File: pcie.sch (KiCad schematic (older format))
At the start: 20 parts

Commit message: sch: Add PCIe power supply
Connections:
- net labels added: +1V5_PCI, +3V3_PCI
- net labels removed: +1V5
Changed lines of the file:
@@
 Connection ~ 3900 2000
 Wire Wire Line
-	2800 2600 2500 2600
-Wire Wire Line
-	2500 2600 2500 1800
+	2800 2600 2400 2600
+Wire Wire Line
+	2400 2600 2400 1800
 $Comp
 L power:+12V #PWR?
@@
 	1    0    0    -1
 $EndComp
-$Comp
-L power:+3V3 #PWR?
-U 1 1 5C9785AC
-P 2500 1800
-F 0 "#PWR?" H 2500 1650 50  0001 C CNN
-F 1 "+3V3" H 2515 1973 50  0000 C CNN
-F 2 "" H 2500 1800 50  0001 C CNN
-F 3 "" H 2500 1800 50  0001 C CNN
-	1    2500 1800
-	1    0    0    -1
-$EndComp
-Wire Wire Line
-	2800 2800 2500 2800
-Wire Wire Line
-	2500 2800 2500 2600
-Connection ~ 2500 2600
+Wire Wire Line
+	2800 2800 2400 2800
+Wire Wire Line
+	2400 2800 2400 2600
+Connection ~ 2400 2600
 $Comp
 L power:+12V #PWR?
@@
 	1    0    0    -1
 $EndComp
-$Comp
-L power:+3V3 #PWR?
-U 1 1 5C9785BB
-P 4100 1800
-F 0 "#PWR?" H 4100 1650 50  0001 C CNN
-F 1 "+3V3" H 4115 1973 50  0000 C CNN
-F 2 "" H 4100 1800 50  0001 C CNN
-F 3 "" H 4100 1800 50  0001 C CNN
-	1    4100 1800
-	1    0    0    -1
-$EndComp
-Wire Wire Line
-	3800 2700 4100 2700
-Wire Wire Line
-	4100 2700 4100 1800
-Wire Wire Line
-	3800 2800 4100 2800
-Wire Wire Line
-	4100 2800 4100 2700
-Connection ~ 4100 2700
+Wire Wire Line
+	3800 2700 4200 2700
+Wire Wire Line
+	4200 2700 4200 1800
+Wire Wire Line
+	3800 2800 4200 2800
+Wire Wire Line
+	4200 2800 4200 2700
+Connection ~ 4200 2700
 Wire Wire Line
 	8100 3000 6550 3000
@@
 Wire Wire Line
 	10150 3200 9400 3200
-Text Label 9850 3100 0    50   ~ 0
+Text Label 9750 3100 0    50   ~ 0
 SCL
-Text Label 9850 3200 0    50   ~ 0
+Text Label 9750 3200 0    50   ~ 0
 SDA
 Wire Bus Line
@@
 Wire Wire Line
 	3800 1900 4550 1900
-Text Label 4150 1900 0    50   ~ 0
+Text Label 4250 1900 0    50   ~ 0
 X4_PRSNT
 $Comp
@@
 Connection ~ 9600 2100
 Wire Wire Line
-	9400 4500 9600 4500
-Wire Wire Line
-	9600 4500 9600 4400
-Wire Wire Line
-	9800 4700 9800 4400
-Wire Wire Line
-	9400 4700 9800 4700
-Wire Wire Line
-	9400 2300 9800 2300
-Wire Wire Line
-	9800 2300 9800 2000
-Wire Wire Line
-	9400 3300 9800 3300
-Wire Wire Line
-	9800 3300 9800 2300
-Connection ~ 9800 2300
-$Comp
-L power:+3V3 #PWR?
-U 1 1 5CE76BBF
-P 7900 2000
-F 0 "#PWR?" H 7900 1850 50  0001 C CNN
-F 1 "+3V3" H 7915 2173 50  0000 C CNN
-F 2 "" H 7900 2000 50  0001 C CNN
-F 3 "" H 7900 2000 50  0001 C CNN
-	1    7900 2000
-	1    0    0    -1
-$EndComp
-$Comp
-L power:+3V3 #PWR?
-U 1 1 5CE76C0A
-P 9600 2000
-F 0 "#PWR?" H 9600 1850 50  0001 C CNN
-F 1 "+3V3" H 9615 2173 50  0000 C CNN
-F 2 "" H 9600 2000 50  0001 C CNN
-F 3 "" H 9600 2000 50  0001 C CNN
-	1    9600 2000
-	1    0    0    -1
-$EndComp
-$Comp
-L power:+3V3 #PWR?
-U 1 1 5CE76DDC
-P 9800 4400
-F 0 "#PWR?" H 9800 4250 50  0001 C CNN
-F 1 "+3V3" H 9815 4573 50  0000 C CNN
-F 2 "" H 9800 4400 50  0001 C CNN
-F 3 "" H 9800 4400 50  0001 C CNN
-	1    9800 4400
-	1    0    0    -1
-$EndComp
-$Comp
-L power:+1V5 #PWR?
-U 1 1 5CE77015
-P 9600 4400
-F 0 "#PWR?" H 9600 4250 50  0001 C CNN
-F 1 "+1V5" H 9615 4573 50  0000 C CNN
-F 2 "" H 9600 4400 50  0001 C CNN
-F 3 "" H 9600 4400 50  0001 C CNN
-	1    9600 4400
-	1    0    0    -1
-$EndComp
-$Comp
-L power:+1V5 #PWR?
-U 1 1 5CE77060
-P 9800 2000
-F 0 "#PWR?" H 9800 1850 50  0001 C CNN
-F 1 "+1V5" H 9815 2173 50  0000 C CNN
-F 2 "" H 9800 2000 50  0001 C CNN
-F 3 "" H 9800 2000 50  0001 C CNN
-	1    9800 2000
-	1    0    0    -1
-$EndComp
+	9400 4500 9700 4500
+Wire Wire Line
+	9700 4500 9700 4400
+Wire Wire Line
+	10100 4700 10100 4400
+Wire Wire Line
+	9400 4700 10100 4700
+Wire Wire Line
+	9400 2300 10000 2300
+Wire Wire Line
+	10000 2300 10000 2000
+Wire Wire Line
+	9400 3300 10000 3300
+Wire Wire Line
+	10000 3300 10000 2300
+Connection ~ 10000 2300
 NoConn ~ 8100 3700
 NoConn ~ 8100 3800
@@
 Text Label 2800 7300 0    50   ~ 0
 nRST
+$Comp
+L pimouss-motherboard:+1V5_PCI #PWR?
+U 1 1 5D12D8FD
+P 10000 2000
+F 0 "#PWR?" H 10000 1850 50  0001 C CNN
+F 1 "+1V5_PCI" H 10015 2173 50  0000 C CNN
+F 2 "" H 10000 2000 50  0001 C CNN
+F 3 "" H 10000 2000 50  0001 C CNN
+	1    10000 2000
+	1    0    0    -1
+$EndComp
+$Comp
+L pimouss-motherboard:+3V3_PCI #PWR?
+U 1 1 5D12DD9A
+P 9600 2000
+F 0 "#PWR?" H 9600 1850 50  0001 C CNN
+F 1 "+3V3_PCI" H 9615 2173 50  0000 C CNN
+F 2 "" H 9600 2000 50  0001 C CNN
+F 3 "" H 9600 2000 50  0001 C CNN
+	1    9600 2000
+	1    0    0    -1
+$EndComp
+$Comp
+L pimouss-motherboard:+3V3_PCI #PWR?
+U 1 1 5D14D95E
+P 7900 2000
+F 0 "#PWR?" H 7900 1850 50  0001 C CNN
+F 1 "+3V3_PCI" H 7915 2173 50  0000 C CNN
+F 2 "" H 7900 2000 50  0001 C CNN
+F 3 "" H 7900 2000 50  0001 C CNN
+	1    7900 2000
+	1    0    0    -1
+$EndComp
+$Comp
+L pimouss-motherboard:+1V5_PCI #PWR?
+U 1 1 5D153F7A
+P 9700 4400
+F 0 "#PWR?" H 9700 4250 50  0001 C CNN
+F 1 "+1V5_PCI" H 9715 4573 50  0000 C CNN
+F 2 "" H 9700 4400 50  0001 C CNN
+F 3 "" H 9700 4400 50  0001 C CNN
+	1    9700 4400
+	1    0    0    -1
+$EndComp
+$Comp
+L pimouss-motherboard:+3V3_PCI #PWR?
+U 1 1 5D166E21
+P 10100 4400
+F 0 "#PWR?" H 10100 4250 50  0001 C CNN
+F 1 "+3V3_PCI" H 10115 4573 50  0000 C CNN
+F 2 "" H 10100 4400 50  0001 C CNN
+F 3 "" H 10100 4400 50  0001 C CNN
+	1    10100 4400
+	1    0    0    -1
+$EndComp
+$Comp
+L pimouss-motherboard:+3V3_PCI #PWR?
+U 1 1 5D1747BC
+P 4200 1800
+F 0 "#PWR?" H 4200 1650 50  0001 C CNN
+F 1 "+3V3_PCI" H 4215 1973 50  0000 C CNN
+F 2 "" H 4200 1800 50  0001 C CNN
+F 3 "" H 4200 1800 50  0001 C CNN
+	1    4200 1800
+	1    0    0    -1
+$EndComp
+$Comp
+L pimouss-motherboard:+3V3_PCI #PWR?
+U 1 1 5D174907
+P 2400 1800
+F 0 "#PWR?" H 2400 1650 50  0001 C CNN
+F 1 "+3V3_PCI" H 2415 1973 50  0000 C CNN
+F 2 "" H 2400 1800 50  0001 C CNN
+F 3 "" H 2400 1800 50  0001 C CNN
+	1    2400 1800
+	1    0    0    -1
+$EndComp
 Wire Bus Line
 	6450 2900 6450 4100

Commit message: sch: Misc fixes
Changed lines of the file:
@@
 $Descr A4 11693 8268
 encoding utf-8
-Sheet 8 9
+Sheet 8 10
 Title "PCI Express connectors"
 Date "2019-03-19"
@@
 Entry Wire Line
 	6450 3000 6550 3100
-Text Label 6100 2900 0    50   ~ 0
+Text Label 6050 2900 0    50   ~ 0
 PCIE_1X
 Wire Wire Line
@@
 Entry Wire Line
 	1950 3600 2050 3700
-Text Label 1600 3500 0    50   ~ 0
+Text Label 1550 3500 0    50   ~ 0
 PCIE_4X
 Wire Wire Line
@@
 Entry Wire Line
 	5450 3800 5350 3900
-Text Label 5800 3400 2    50   ~ 0
+Text Label 5850 3400 2    50   ~ 0
 PCIE_4X
 Text Label 5300 3500 2    50   ~ 0
@@
 Wire Bus Line
 	10250 3000 10650 3000
-Text Label 10600 3000 2    50   ~ 0
+Text Label 10650 3000 2    50   ~ 0
 SMBUS
 Wire Bus Line
 	1950 2200 1550 2200
-Text Label 1600 2200 0    50   ~ 0
+Text Label 1550 2200 0    50   ~ 0
 SMBUS
 NoConn ~ 3800 2300
@@
 Wire Wire Line
 	10150 3600 9400 3600
-Text Label 9850 3600 0    50   ~ 0
+Text Label 10150 3600 2    50   ~ 0
 nRST
 Wire Wire Line
-	4550 2900 3800 2900
-Text Label 4250 2900 0    50   ~ 0
+	4650 2900 3800 2900
+Text Label 4650 2900 2    50   ~ 0
 nRST
 NoConn ~ 2800 2900
@@
 Wire Wire Line
 	2800 5700 2050 5700
-Text Label 2150 5700 0    50   ~ 0
+Text Label 2050 5700 0    50   ~ 0
 X4_PRSNT
 Wire Wire Line
-	3800 1900 4550 1900
-Text Label 4250 1900 0    50   ~ 0
+	3800 1900 4650 1900
+Text Label 4650 1900 2    50   ~ 0
 X4_PRSNT
 $Comp
@@
 Wire Bus Line
 	3100 7000 2700 7000
-Text Label 2750 7000 0    50   ~ 0
+Text Label 3100 7000 2    50   ~ 0
 PCIE_1X
 Wire Bus Line
 	3100 7100 2700 7100
-Text Label 2750 7100 0    50   ~ 0
+Text Label 3100 7100 2    50   ~ 0
 PCIE_4X
 Wire Bus Line
 	3100 7200 2700 7200
-Text Label 2750 7200 0    50   ~ 0
+Text Label 3100 7200 2    50   ~ 0
 SMBUS
 Wire Wire Line
 	2700 7300 3100 7300
-Text Label 2800 7300 0    50   ~ 0
+Text Label 3100 7300 2    50   ~ 0
 nRST
 $Comp

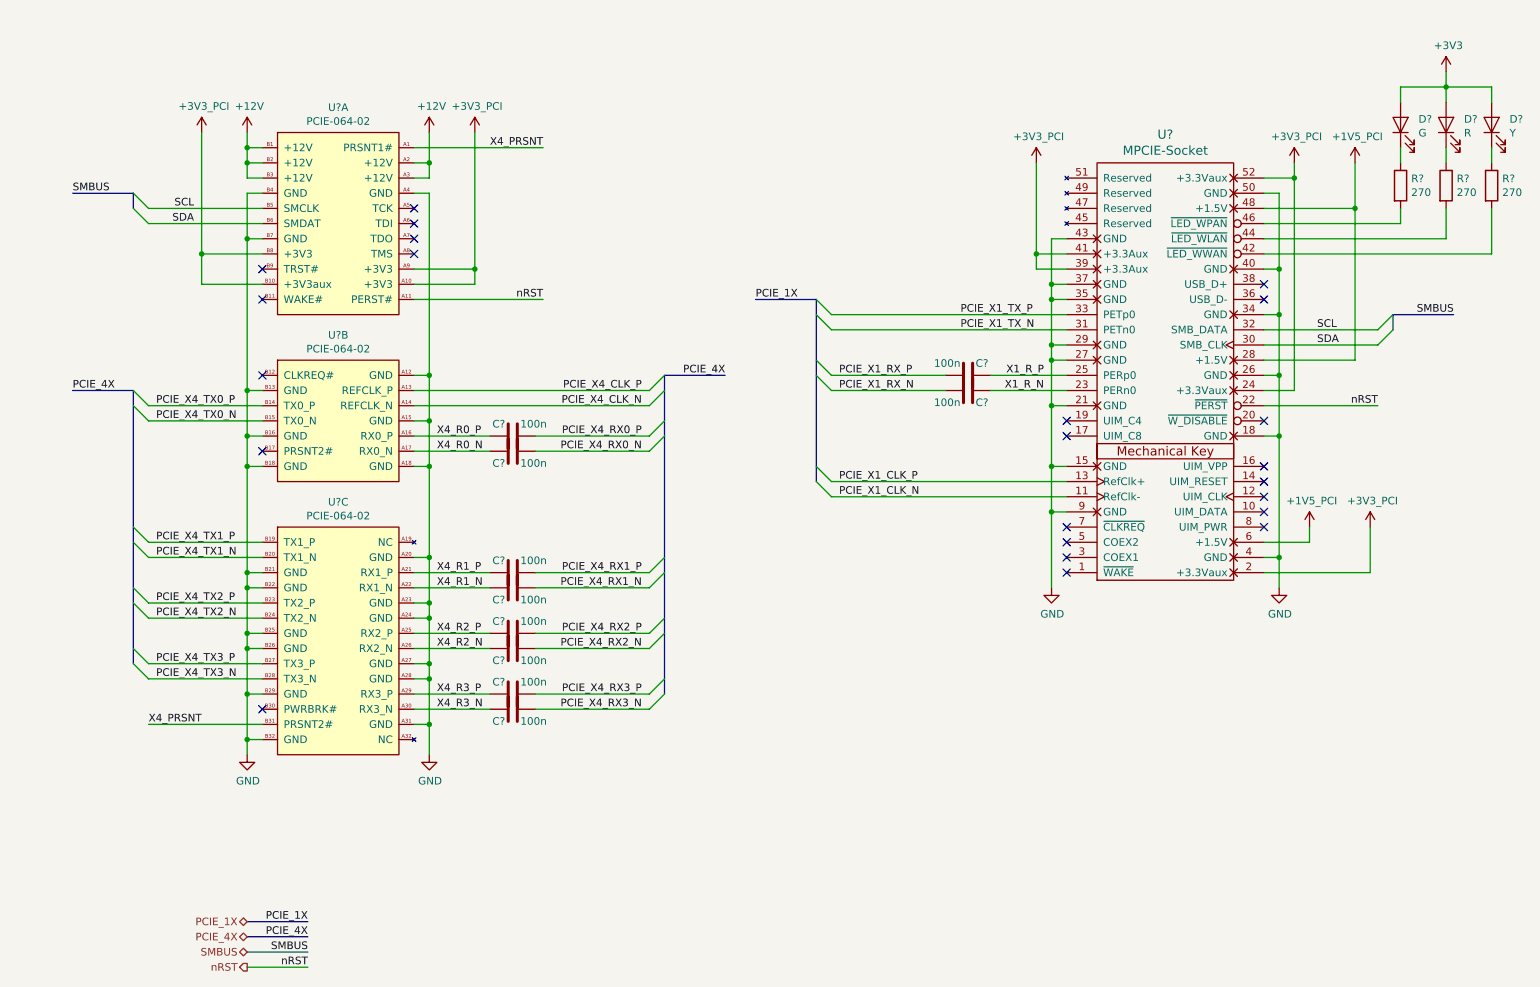
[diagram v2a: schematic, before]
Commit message: sch: Add second mPCIe port with PCIe switch
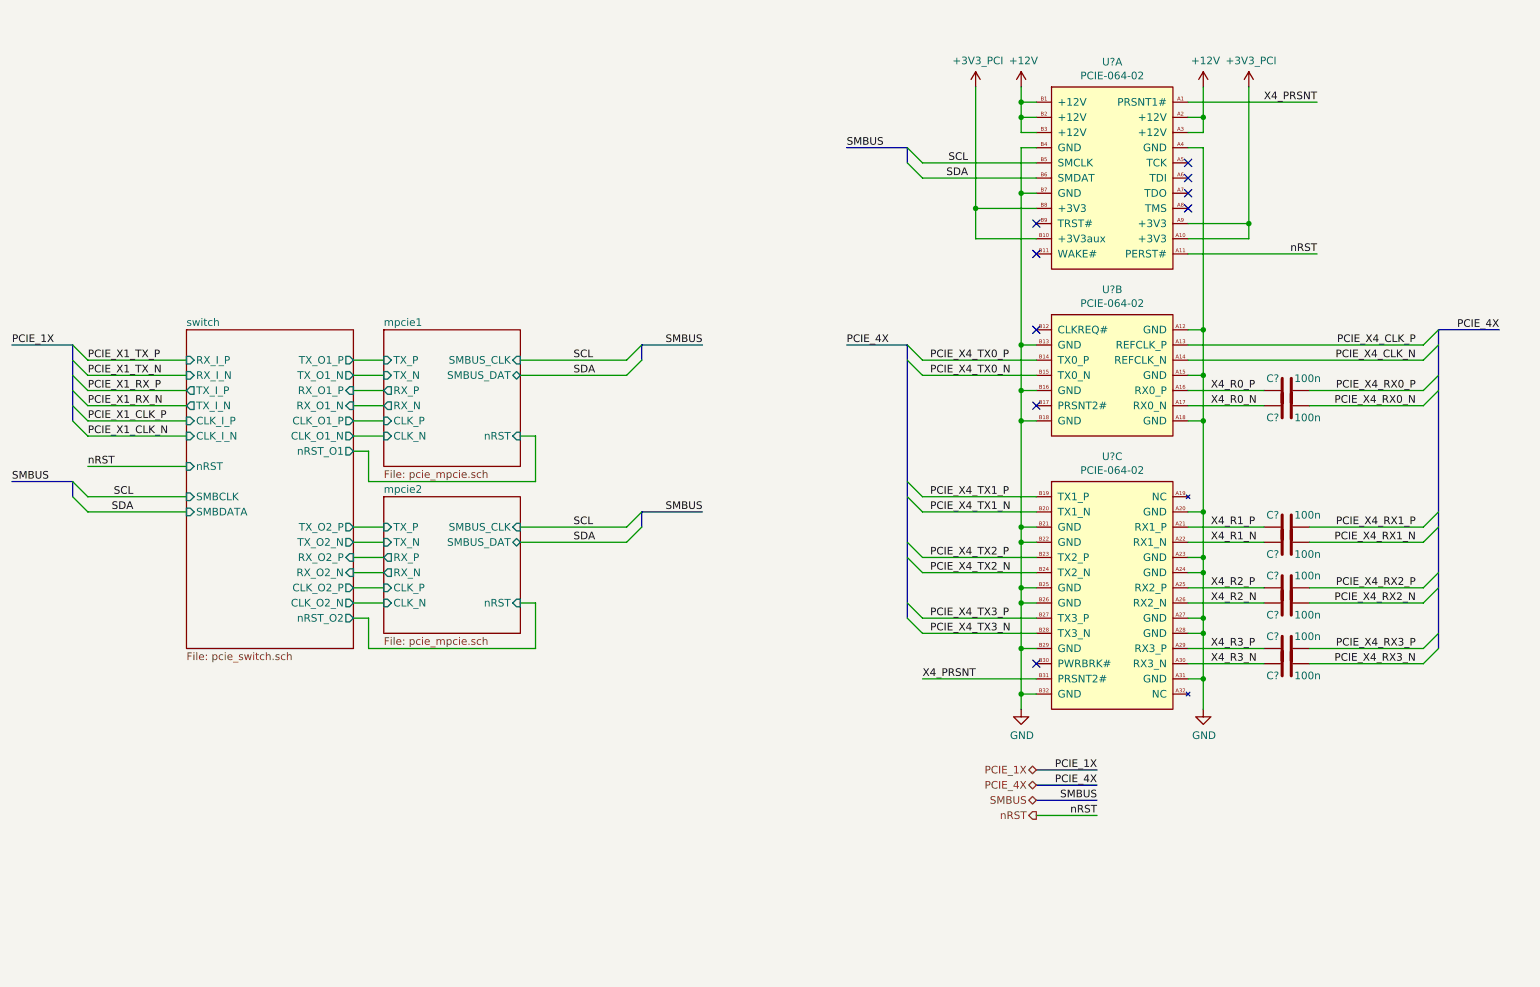
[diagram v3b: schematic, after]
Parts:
- removed C? (x2): 100n, symbol Device:C
- removed D?: G, symbol Device:LED
- removed D?: R, symbol Device:LED
- removed D?: Y, symbol Device:LED
- removed R? (x3): 270, symbol Device:R
- removed U?: MPCIE-Socket, symbol mpcie:MPCIE-Socket
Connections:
- no-connect marks 23 -> 9
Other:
- moved on the sheet: C?, U?A, U?B, U?C

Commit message: sch: Add some PCIe doc and termination resistors
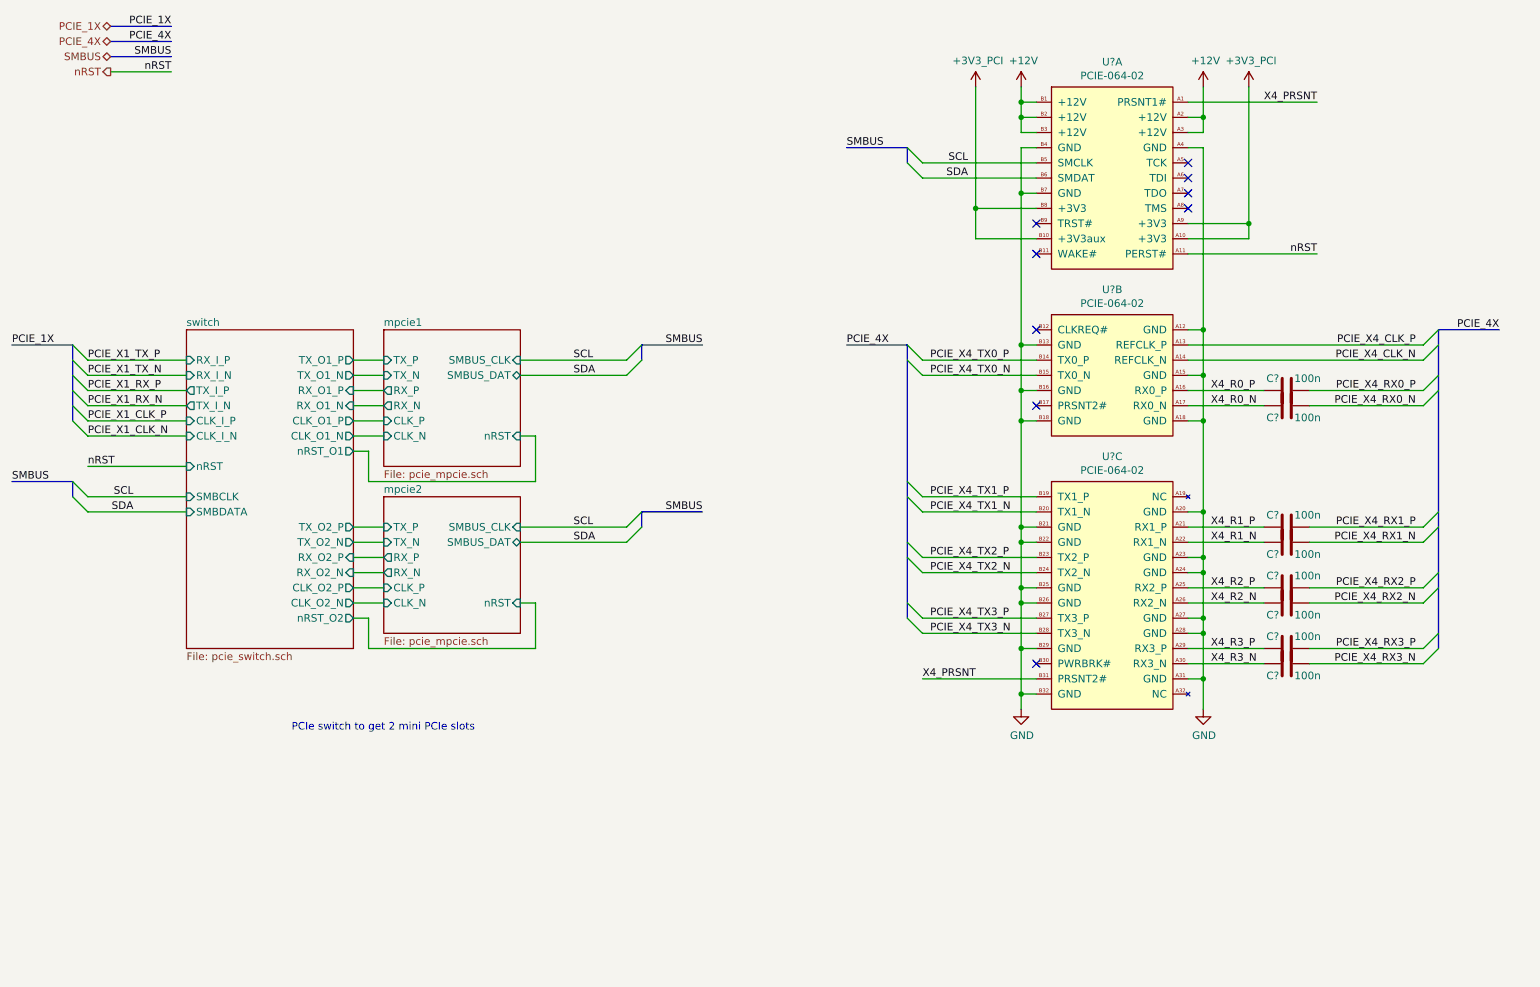
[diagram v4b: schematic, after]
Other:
- note added: "PCIe switch to get 2 mini PCIe slots"
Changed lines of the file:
@@
 Wire Wire Line
 	8900 3300 10450 3300
-Text HLabel 7900 6000 0    50   BiDi ~ 0
+Text HLabel 1800 1100 0    50   BiDi ~ 0
 PCIE_1X
-Text HLabel 7900 6100 0    50   BiDi ~ 0
+Text HLabel 1800 1200 0    50   BiDi ~ 0
 PCIE_4X
-Text HLabel 7900 6200 0    50   BiDi ~ 0
-SMBUS
-Text HLabel 7900 6300 0    50   Output ~ 0
+Text HLabel 1800 1300 0    50   BiDi ~ 0
+SMBUS
+Text HLabel 1800 1400 0    50   Output ~ 0
 nRST
 Wire Bus Line
-	8300 6000 7900 6000
-Text Label 8300 6000 2    50   ~ 0
+	2200 1100 1800 1100
+Text Label 2200 1100 2    50   ~ 0
 PCIE_1X
 Wire Bus Line
-	8300 6100 7900 6100
-Text Label 8300 6100 2    50   ~ 0
+	2200 1200 1800 1200
+Text Label 2200 1200 2    50   ~ 0
 PCIE_4X
 Wire Bus Line
-	8300 6200 7900 6200
-Text Label 8300 6200 2    50   ~ 0
-SMBUS
-Wire Wire Line
-	7900 6300 8300 6300
-Text Label 8300 6300 2    50   ~ 0
+	2200 1300 1800 1300
+Text Label 2200 1300 2    50   ~ 0
+SMBUS
+Wire Wire Line
+	1800 1400 2200 1400
+Text Label 2200 1400 2    50   ~ 0
 nRST
 $Comp
@@
 Text Label 1150 4100 0    50   ~ 0
 SMBUS
+Text Notes 4200 5750 2    50   ~ 0
+PCIe switch to get 2 mini PCIe slots
 Wire Bus Line
 	1550 3200 1550 3700
